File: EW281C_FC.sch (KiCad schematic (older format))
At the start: 5 parts, among them J13 USB_B_Micro

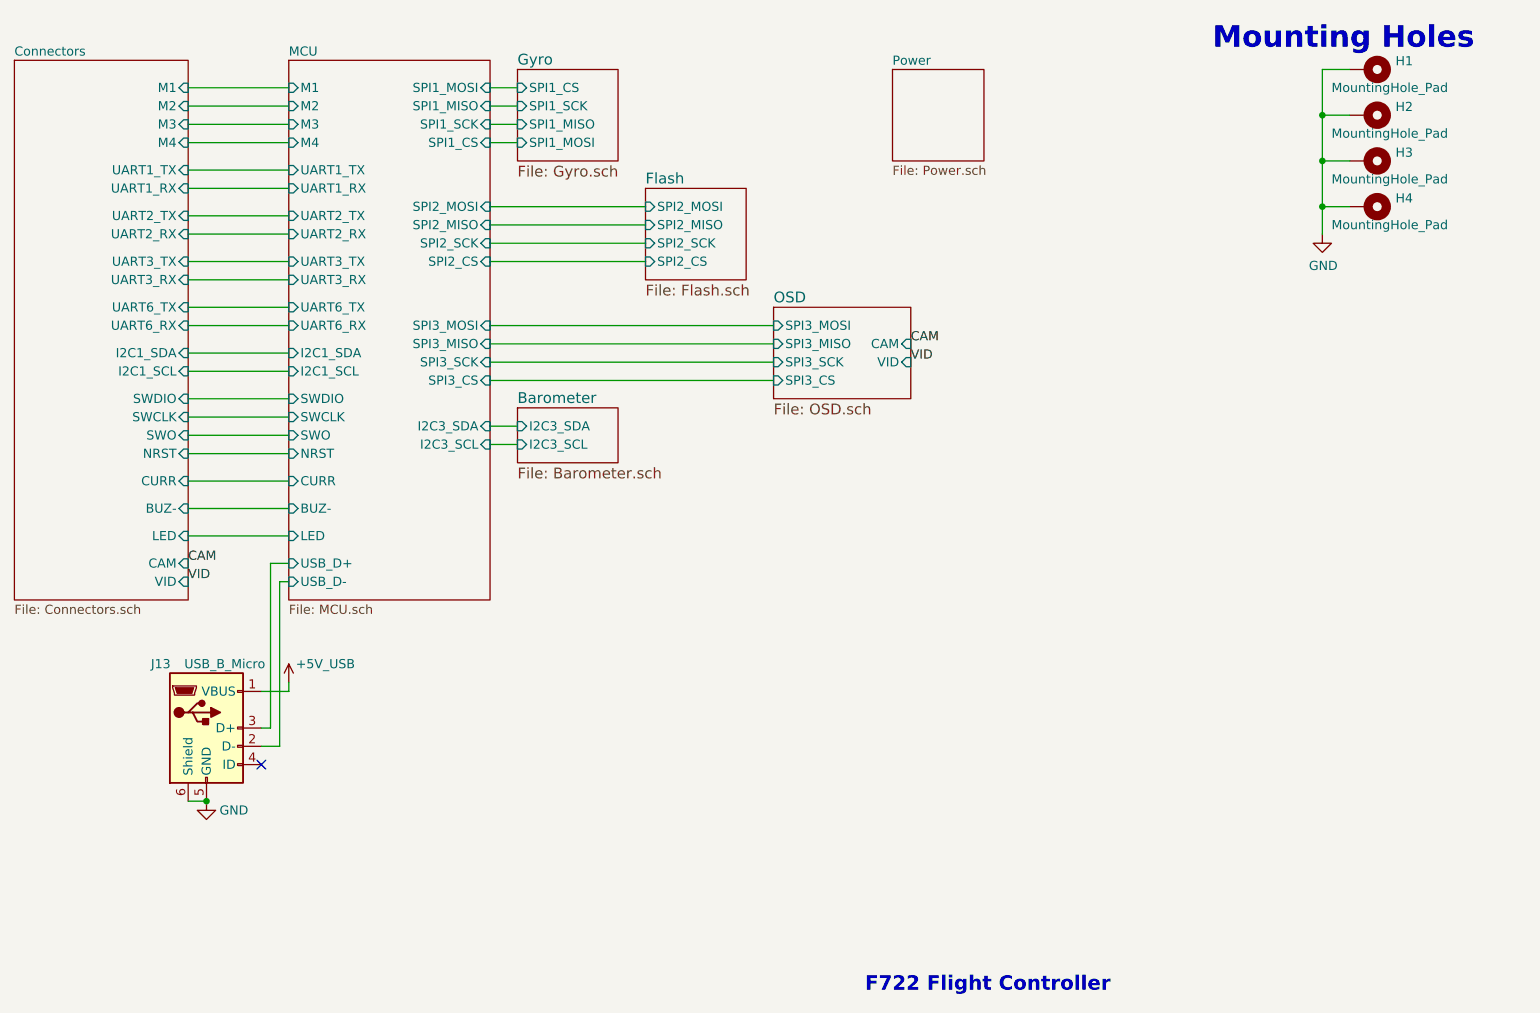
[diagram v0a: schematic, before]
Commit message: Changed to 20x20 form factor
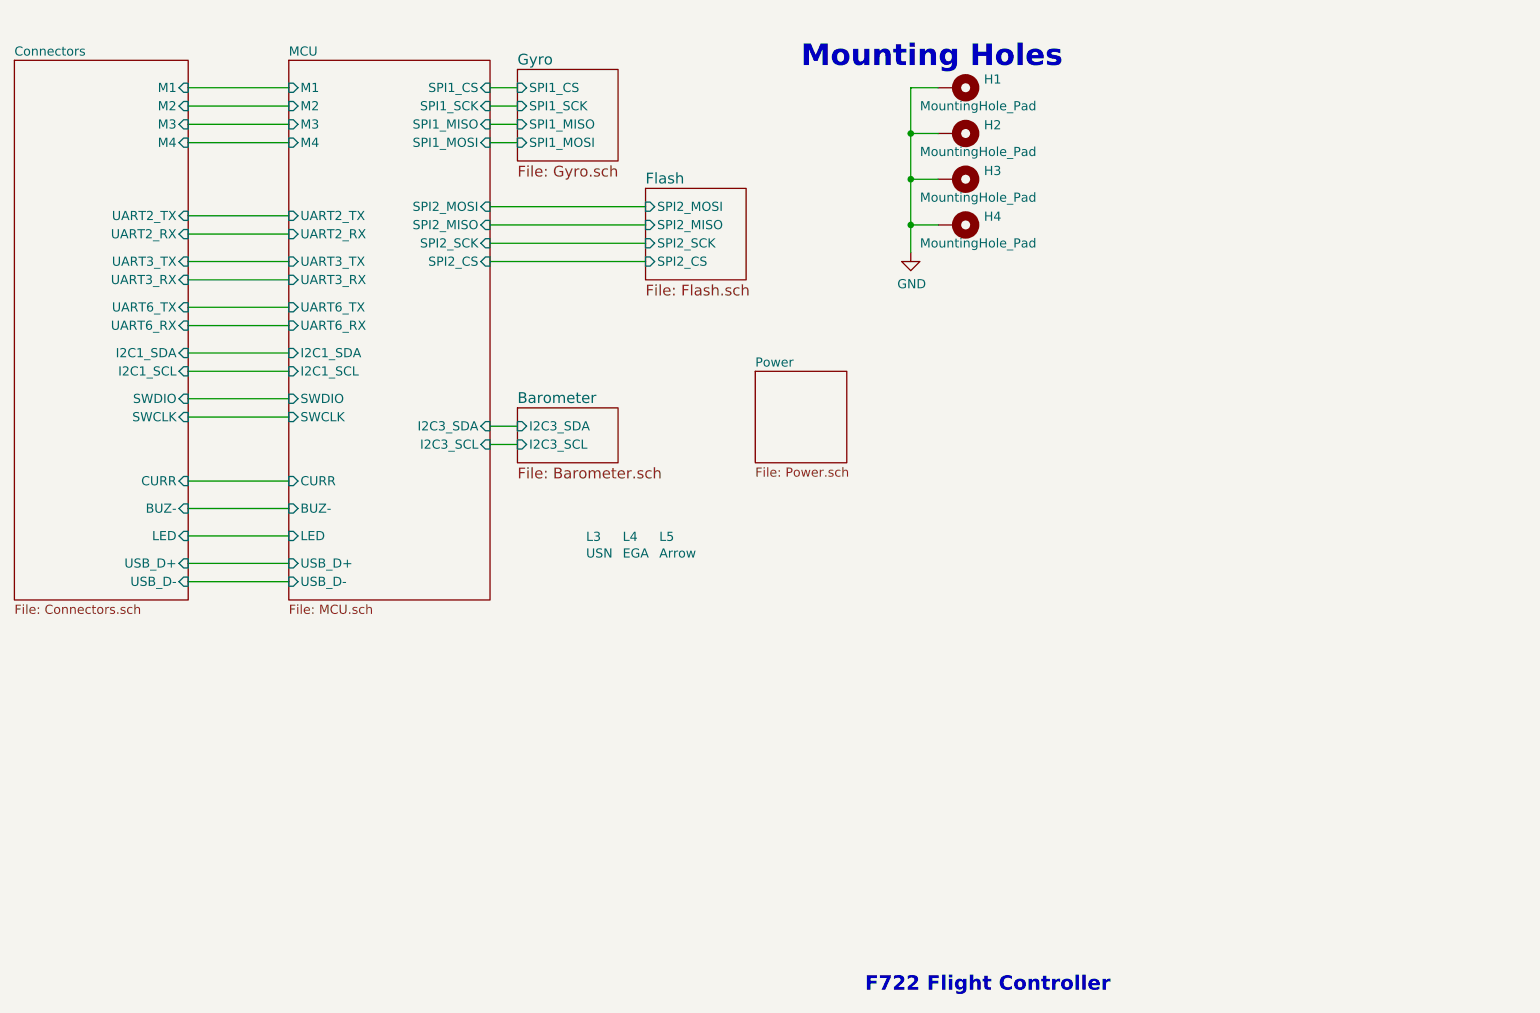
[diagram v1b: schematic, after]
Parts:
- removed J13: USB_B_Micro, Connector_USB:USB_Micro-B_Amphenol_10103594-0001LF_Horizontal, symbol Connector:USB_B_Micro
- added L3: USN, Footprints:USN, symbol Logos:USN
- added L4: EGA, Footprints:EGA, symbol Logos:EGA
- added L5: Arrow, Footprints:Arrow, symbol Logos:Arrow
- H1, H2, H3, H4: footprint MountingHole:MountingHole_2.7mm_Pad -> MountingHole:MountingHole_3mm_M2_20x20
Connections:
- no-connect marks 1 -> 0
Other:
- moved on the sheet: H1

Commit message: Changes made
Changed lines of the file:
@@
 F20 "I2C3_SDA" I R 5300 4400 50
 F21 "M2" I L 4200 2650 50
-F22 "UART6_RX" I L 4200 3850 50
-F23 "UART6_TX" I L 4200 3750 50
-F24 "CURR" I L 4200 4700 50
-F25 "BUZ-" I L 4200 4850 50
-F26 "I2C1_SCL" I L 4200 4100 50
-F27 "I2C1_SDA" I L 4200 4000 50
-F28 "USB_D-" I L 4200 5250 50
-F29 "USB_D+" I L 4200 5150 50
-F30 "LED" I L 4200 5000 50
+F22 "CURR" I L 4200 4700 50
+F23 "BUZ-" I L 4200 4850 50
+F24 "I2C1_SCL" I L 4200 4100 50
+F25 "I2C1_SDA" I L 4200 4000 50
+F26 "USB_D-" I L 4200 5250 50
+F27 "USB_D+" I L 4200 5150 50
+F28 "LED" I L 4200 5000 50
+F29 "UART6_RX" I L 4200 3750 50
 $EndSheet
 $Sheet
@@
 Wire Wire Line
 	3650 3600 4200 3600
-Wire Wire Line
-	3650 3750 4200 3750
-Wire Wire Line
-	3650 3850 4200 3850
 Wire Wire Line
 	3650 2550 4200 2550
@@
 F10 "UART2_RX" I R 3650 3350 50
 F11 "UART2_TX" I R 3650 3250 50
-F12 "UART6_TX" I R 3650 3750 50
-F13 "UART6_RX" I R 3650 3850 50
-F14 "M2" I R 3650 2650 50
-F15 "M1" I R 3650 2550 50
-F16 "M3" I R 3650 2750 50
-F17 "M4" I R 3650 2850 50
-F18 "CURR" I R 3650 4700 50
-F19 "USB_D+" I R 3650 5150 50
-F20 "USB_D-" I R 3650 5250 50
+F12 "M2" I R 3650 2650 50
+F13 "M1" I R 3650 2550 50
+F14 "M3" I R 3650 2750 50
+F15 "M4" I R 3650 2850 50
+F16 "CURR" I R 3650 4700 50
+F17 "USB_D+" I R 3650 5150 50
+F18 "USB_D-" I R 3650 5250 50
+F19 "UART6_RX" I R 3650 3750 50
 $EndSheet
 Wire Wire Line
@@
 Wire Wire Line
 	3650 5250 4200 5250
+Wire Wire Line
+	3650 3750 4200 3750
 $EndSCHEMATC

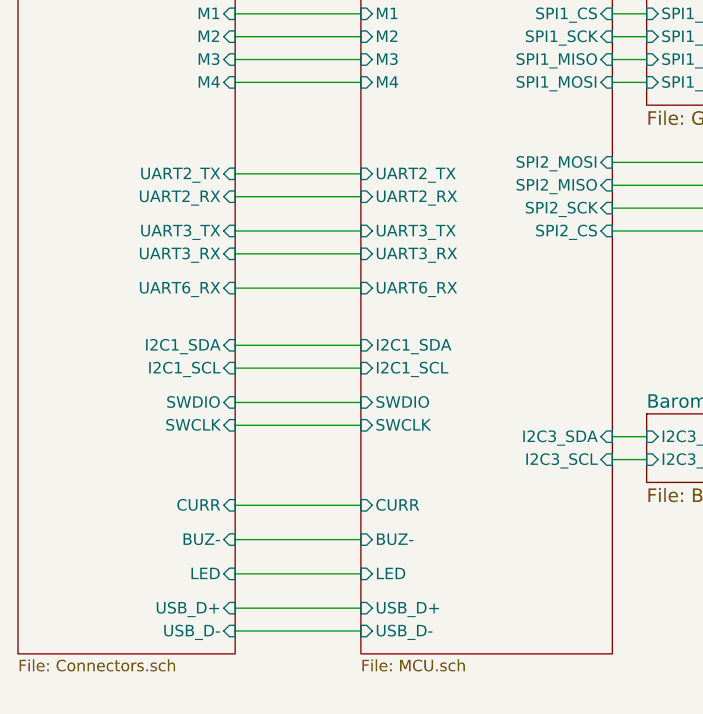
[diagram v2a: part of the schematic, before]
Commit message: Changed some components to match what is in stock
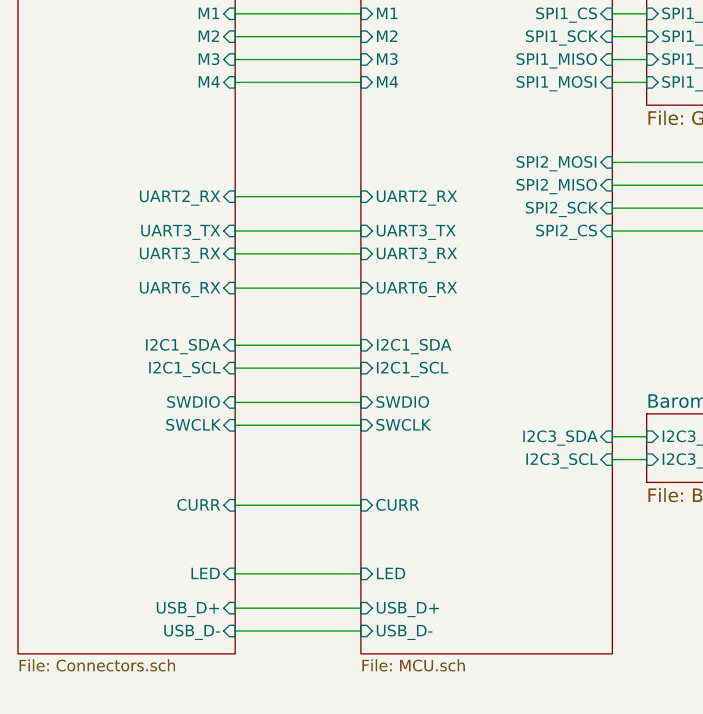
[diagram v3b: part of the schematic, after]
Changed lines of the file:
@@
 F4 "SPI1_MISO" I R 5300 2750 50
 F5 "SPI1_MOSI" I R 5300 2850 50
-F6 "UART2_TX" I L 4200 3250 50
-F7 "UART2_RX" I L 4200 3350 50
-F8 "M1" I L 4200 2550 50
-F9 "I2C3_SCL" I R 5300 4500 50
-F10 "SWDIO" I L 4200 4250 50
-F11 "SWCLK" I L 4200 4350 50
-F12 "M4" I L 4200 2850 50
-F13 "M3" I L 4200 2750 50
-F14 "UART3_TX" I L 4200 3500 50
-F15 "UART3_RX" I L 4200 3600 50
-F16 "SPI2_CS" I R 5300 3500 50
-F17 "SPI2_SCK" I R 5300 3400 50
-F18 "SPI2_MISO" I R 5300 3300 50
-F19 "SPI2_MOSI" I R 5300 3200 50
-F20 "I2C3_SDA" I R 5300 4400 50
-F21 "M2" I L 4200 2650 50
-F22 "CURR" I L 4200 4700 50
-F23 "BUZ-" I L 4200 4850 50
-F24 "I2C1_SCL" I L 4200 4100 50
-F25 "I2C1_SDA" I L 4200 4000 50
-F26 "USB_D-" I L 4200 5250 50
-F27 "USB_D+" I L 4200 5150 50
-F28 "LED" I L 4200 5000 50
-F29 "UART6_RX" I L 4200 3750 50
+F6 "UART2_RX" I L 4200 3350 50
+F7 "M1" I L 4200 2550 50
+F8 "I2C3_SCL" I R 5300 4500 50
+F9 "SWDIO" I L 4200 4250 50
+F10 "SWCLK" I L 4200 4350 50
+F11 "M4" I L 4200 2850 50
+F12 "M3" I L 4200 2750 50
+F13 "UART3_TX" I L 4200 3500 50
+F14 "UART3_RX" I L 4200 3600 50
+F15 "SPI2_CS" I R 5300 3500 50
+F16 "SPI2_SCK" I R 5300 3400 50
+F17 "SPI2_MISO" I R 5300 3300 50
+F18 "SPI2_MOSI" I R 5300 3200 50
+F19 "I2C3_SDA" I R 5300 4400 50
+F20 "M2" I L 4200 2650 50
+F21 "CURR" I L 4200 4700 50
+F22 "I2C1_SCL" I L 4200 4100 50
+F23 "I2C1_SDA" I L 4200 4000 50
+F24 "USB_D-" I L 4200 5250 50
+F25 "USB_D+" I L 4200 5150 50
+F26 "LED" I L 4200 5000 50
+F27 "UART6_RX" I L 4200 3750 50
 $EndSheet
 $Sheet
@@
 $EndSheet
 Wire Wire Line
-	3650 3250 4200 3250
-Wire Wire Line
-	3650 3350 4200 3350
-Wire Wire Line
 	3650 3500 4200 3500
 Wire Wire Line
@@
 Wire Wire Line
 	3650 4350 4200 4350
-Wire Wire Line
-	3650 4850 4200 4850
 Wire Wire Line
 	3650 4700 4200 4700
@@
 F4 "SWCLK" I R 3650 4350 50
 F5 "SWDIO" I R 3650 4250 50
-F6 "BUZ-" I R 3650 4850 50
-F7 "LED" I R 3650 5000 50
-F8 "UART3_RX" I R 3650 3600 50
-F9 "UART3_TX" I R 3650 3500 50
-F10 "UART2_RX" I R 3650 3350 50
-F11 "UART2_TX" I R 3650 3250 50
-F12 "M2" I R 3650 2650 50
-F13 "M1" I R 3650 2550 50
-F14 "M3" I R 3650 2750 50
-F15 "M4" I R 3650 2850 50
-F16 "CURR" I R 3650 4700 50
-F17 "USB_D+" I R 3650 5150 50
-F18 "USB_D-" I R 3650 5250 50
-F19 "UART6_RX" I R 3650 3750 50
+F6 "LED" I R 3650 5000 50
+F7 "UART3_RX" I R 3650 3600 50
+F8 "UART3_TX" I R 3650 3500 50
+F9 "UART2_RX" I R 3650 3350 50
+F10 "M2" I R 3650 2650 50
+F11 "M1" I R 3650 2550 50
+F12 "M3" I R 3650 2750 50
+F13 "M4" I R 3650 2850 50
+F14 "CURR" I R 3650 4700 50
+F15 "USB_D+" I R 3650 5150 50
+F16 "USB_D-" I R 3650 5250 50
+F17 "UART6_RX" I R 3650 3750 50
 $EndSheet
 Wire Wire Line
@@
 Wire Wire Line
 	3650 3750 4200 3750
+Wire Wire Line
+	3650 3350 4200 3350
 $EndSCHEMATC
